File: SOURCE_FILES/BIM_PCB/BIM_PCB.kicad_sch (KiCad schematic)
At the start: 13 parts, among them J1 POWER INPUT, J6 Conn_01x04, Q1 SSM3J328R-HXY

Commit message: updates on schematic and complete layout
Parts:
- removed J6: Conn_01x04, Connector_Phoenix_MC:PhoenixContact_MC_1,5_4-G-3.5_1x04_P3.50mm_Horizontal, symbol Connector_Generic:Conn_01x04
- removed JP4, JP5: Jumper_3_Bridged12, Connector_PinHeader_2.54mm:PinHeader_1x03_P2.54mm_Vertical, symbol Jumper:Jumper_3_Bridged12
- added J6: Conn_02x02_Odd_Even, Connector_Molex:Molex_Mini-Fit_Jr_5569-04A2_2x02_P4.20mm_Horizontal, symbol Connector_Generic:Conn_02x02_Odd_Even
- gave numbers to parts that had none: 4
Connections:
- net +5V: now also J6.2 (Pin_2)
- net GND: now also J6.4 (Pin_4)
- net RS485_MAX485/A: now also J6.1 (Pin_1)
- net RS485_MAX485/B: now also J6.3 (Pin_3)
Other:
- sheet CAN_TRANSCEIVER_ATA6561 ports: added none; removed CANH, CANL
- sheet RS485_MAX485 ports: added RS485_DE, RS485_~{RE}; removed RS485_EN
- sheet SIM7000_GPRS_MODULE ports: added GPS_RXD, GPS_TXD; removed none
- sheet STM32FC8T6_MCU ports: added RS485_DE, RS485_~{RE}; removed RS485_EN

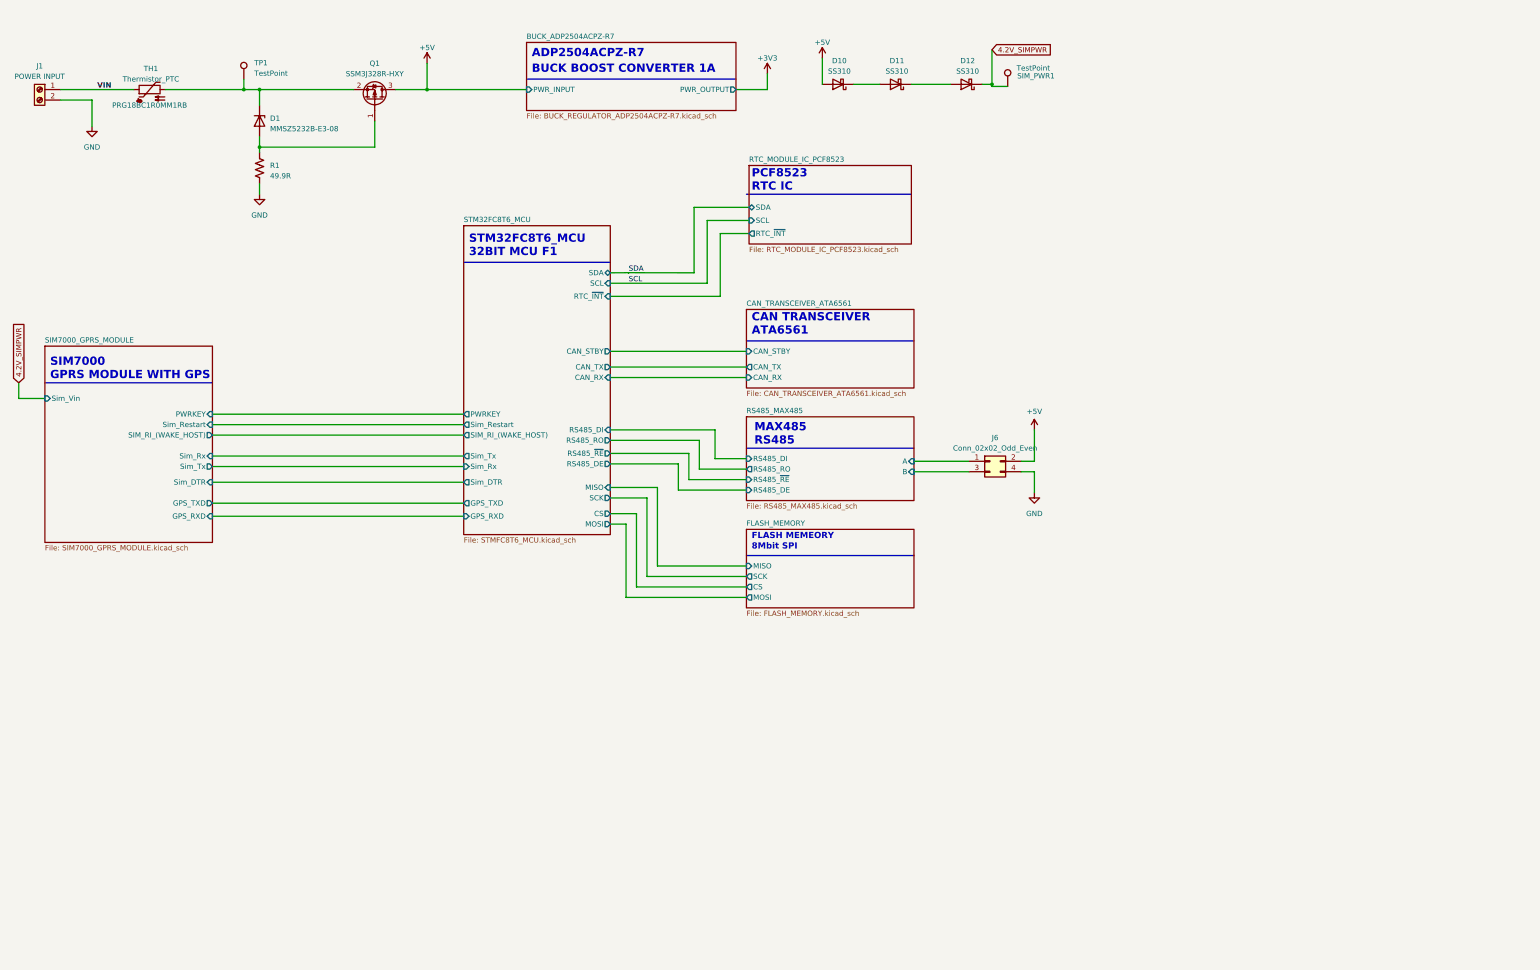
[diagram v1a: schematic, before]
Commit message: completed design PCN and Images
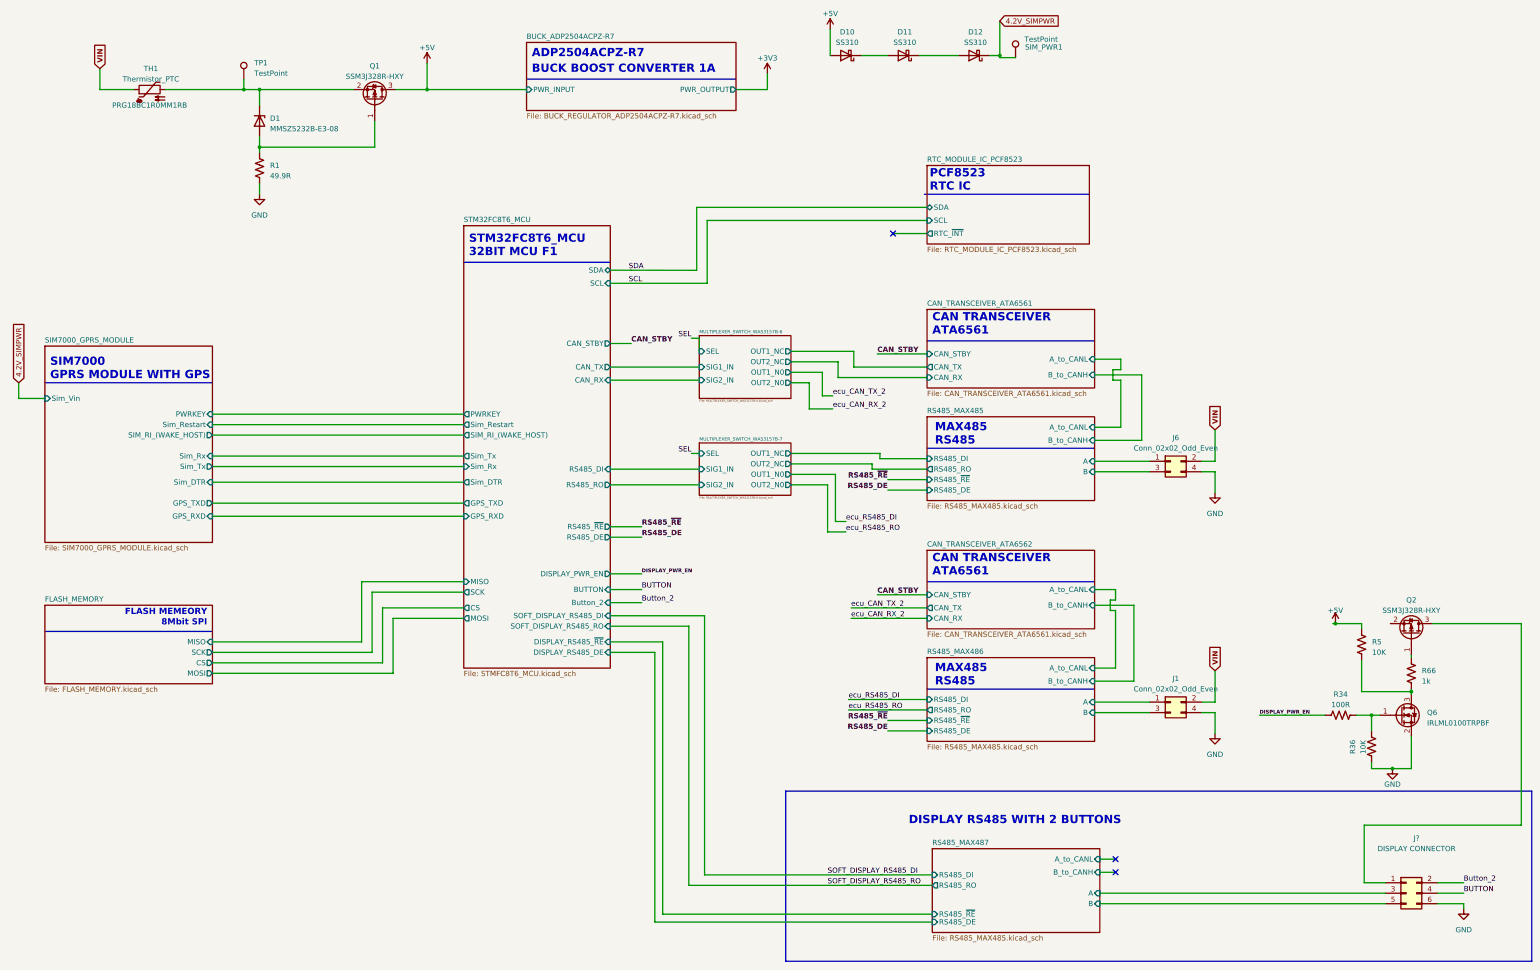
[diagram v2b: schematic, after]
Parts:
- removed J1: POWER INPUT, TerminalBlock_Phoenix:TerminalBlock_Phoenix_PT-1,5-2-3.5-H_1x02_P3.50mm_Horizontal, symbol Connector:Screw_Terminal_01x02
- added J1: Conn_02x02_Odd_Even, Connector_Molex:Molex_Nano-Fit_105314-xx04_2x02_P2.50mm_Horizontal, symbol Connector_Generic:Conn_02x02_Odd_Even
- added J?: DISPLAY CONNECTOR, Connector_Molex:Molex_Nano-Fit_105314-xx06_2x03_P2.50mm_Horizontal, symbol Connector_Generic:Conn_02x03_Odd_Even
- added Q2: SSM3J328R-HXY, Package_TO_SOT_SMD:SOT-23, symbol Device:Q_PMOS_GSD
- added Q6: IRLML0100TRPBF, Package_TO_SOT_SMD:SOT-23, symbol Device:Q_NMOS_GSD
- added R34: 100R, Resistor_SMD:R_0402_1005Metric, symbol Device:R_US
- added R36, R5: 10K, Resistor_SMD:R_0402_1005Metric, symbol Device:R_US
- added R66: 1k, Resistor_SMD:R_0402_1005Metric, symbol Device:R_US
- D1: footprint Diode_SMD:D_MiniMELF -> Diode_SMD:D_SOD-123
- J6: footprint Connector_Molex:Molex_Mini-Fit_Jr_5569-04A2_2x02_P4.20mm_Horizontal -> Connector_Molex:Molex_Nano-Fit_105314-xx04_2x02_P2.50mm_Horizontal
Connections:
- net +5V: now also R5.1; no longer J6.2 (Pin_2)
- net GND: now also J1.4 (Pin_4), J?.6 (Pin_6), Q6.2 (S), R36.2
- net VIN: now also J6.2 (Pin_2), J1.2 (Pin_2)
- new net: Q6.3 (D), R5.2, R66.1
- new net: Q6.1 (G), R34.1, R36.1
- new net: J?.1 (Pin_1), Q2.3 (D)
- new net: Q2.1 (G), R66.2
- new net BUTTON: J?.4 (Pin_4)
- new net Button_2: J?.2 (Pin_2)
- new net DISPLAY_PWR_EN: R34.2
- new net RS485_MAX486/A: J1.1 (Pin_1)
- new net RS485_MAX486/B: J1.3 (Pin_3)
- new net RS485_MAX487/A: J?.3 (Pin_3)
- new net RS485_MAX487/B: J?.5 (Pin_5)
- no-connect marks 0 -> 3
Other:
- added sheet CAN_TRANSCEIVER_ATA6562 (CAN_TRANSCEIVER_ATA6561.kicad_sch)
- added sheet MULTIPLEXER_SWITCH_WAS3157B-6 (MULTIPLEXER_SWITCH_WAS3157B-6.kicad_sch)
- added sheet MULTIPLEXER_SWITCH_WAS3157B-7 (MULTIPLEXER_SWITCH_WAS3157B-6.kicad_sch)
- added sheet RS485_MAX486 (RS485_MAX485.kicad_sch)
- added sheet RS485_MAX487 (RS485_MAX485.kicad_sch)
- sheet CAN_TRANSCEIVER_ATA6561 ports: added A_to_CANL, B_to_CANH; removed none
- sheet RS485_MAX485 ports: added A_to_CANL, B_to_CANH; removed none
- sheet STM32FC8T6_MCU ports: added BUTTON, Button_2, DISPLAY_PWR_EN, DISPLAY_RS485_DE, DISPLAY_RS485_~{RE}, SOFT_DISPLAY_RS485_DI, SOFT_DISPLAY_RS485_RO; removed RTC_~{INT}
- note added: "DISPLAY RS485 WITH 2 BUTTONS"
- moved on the sheet: D10, D11, D12, J6, SIM_PWR1

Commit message: complete BIM Board
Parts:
- added C45, C46: 100n, Capacitor_SMD:C_0603_1608Metric, symbol Device:C_Small
- added U14, U15: MC74HC4052A, Package_SO:SSOP-16_5.3x6.2mm_P0.65mm, symbol MCD_General:MC74HC4052A
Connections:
- net +3V3: now also C45.1, C46.1, U14.16 (VCC), U14.7 (VEE), U15.16 (VCC), U15.7 (VEE)
- net +5V: now also Q2.2 (S)
- net GND: now also C45.2, C46.2, U14.6 (ENABLE), U14.8 (GND), U15.6 (ENABLE), U15.8 (GND)
- net ecu_CAN_RX_2: now also U14.14 (X1)
- net ecu_CAN_TX_2: now also U14.5 (Y1)
- net ecu_RS485_DI: now also U15.5 (Y1)
- net ecu_RS485_RO: now also U15.14 (X1)
- new net CAN_RX_2: U14.12 (X0)
- new net CAN_TX_2: U14.1 (Y0)
- new net DISPLAY_RS485_DI: U15.2 (Y2)
- new net DISPLAY_RS485_RO: U15.15 (X2)
- new net MUX_SEL_A: U14.10 (A), U15.10 (A)
- new net MUX_SEL_B: U14.9 (B), U15.9 (B)
- new net RS485_D1: U15.1 (Y0)
- new net RS485_RO: U15.12 (X0)
- new net STM32FC8T6_MCU/CAN_RX: U14.13 (X)
- new net STM32FC8T6_MCU/CAN_TX: U14.3 (Y)
- new net STM32FC8T6_MCU/RS485_DI: U15.3 (Y)
- new net STM32FC8T6_MCU/RS485_RO: U15.13 (X)
- no-connect marks 3 -> 9
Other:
- removed sheet MULTIPLEXER_SWITCH_WAS3157B-6
- removed sheet MULTIPLEXER_SWITCH_WAS3157B-7
- sheet STM32FC8T6_MCU ports: added MUX_SEL_A, MUX_SEL_B, SEL; removed DISPLAY_RS485_DE, DISPLAY_RS485_~{RE}, SOFT_DISPLAY_RS485_DI, SOFT_DISPLAY_RS485_RO
- moved on the sheet: J1, J6, J?, Q2, Q6, R34, R36, R5, R66

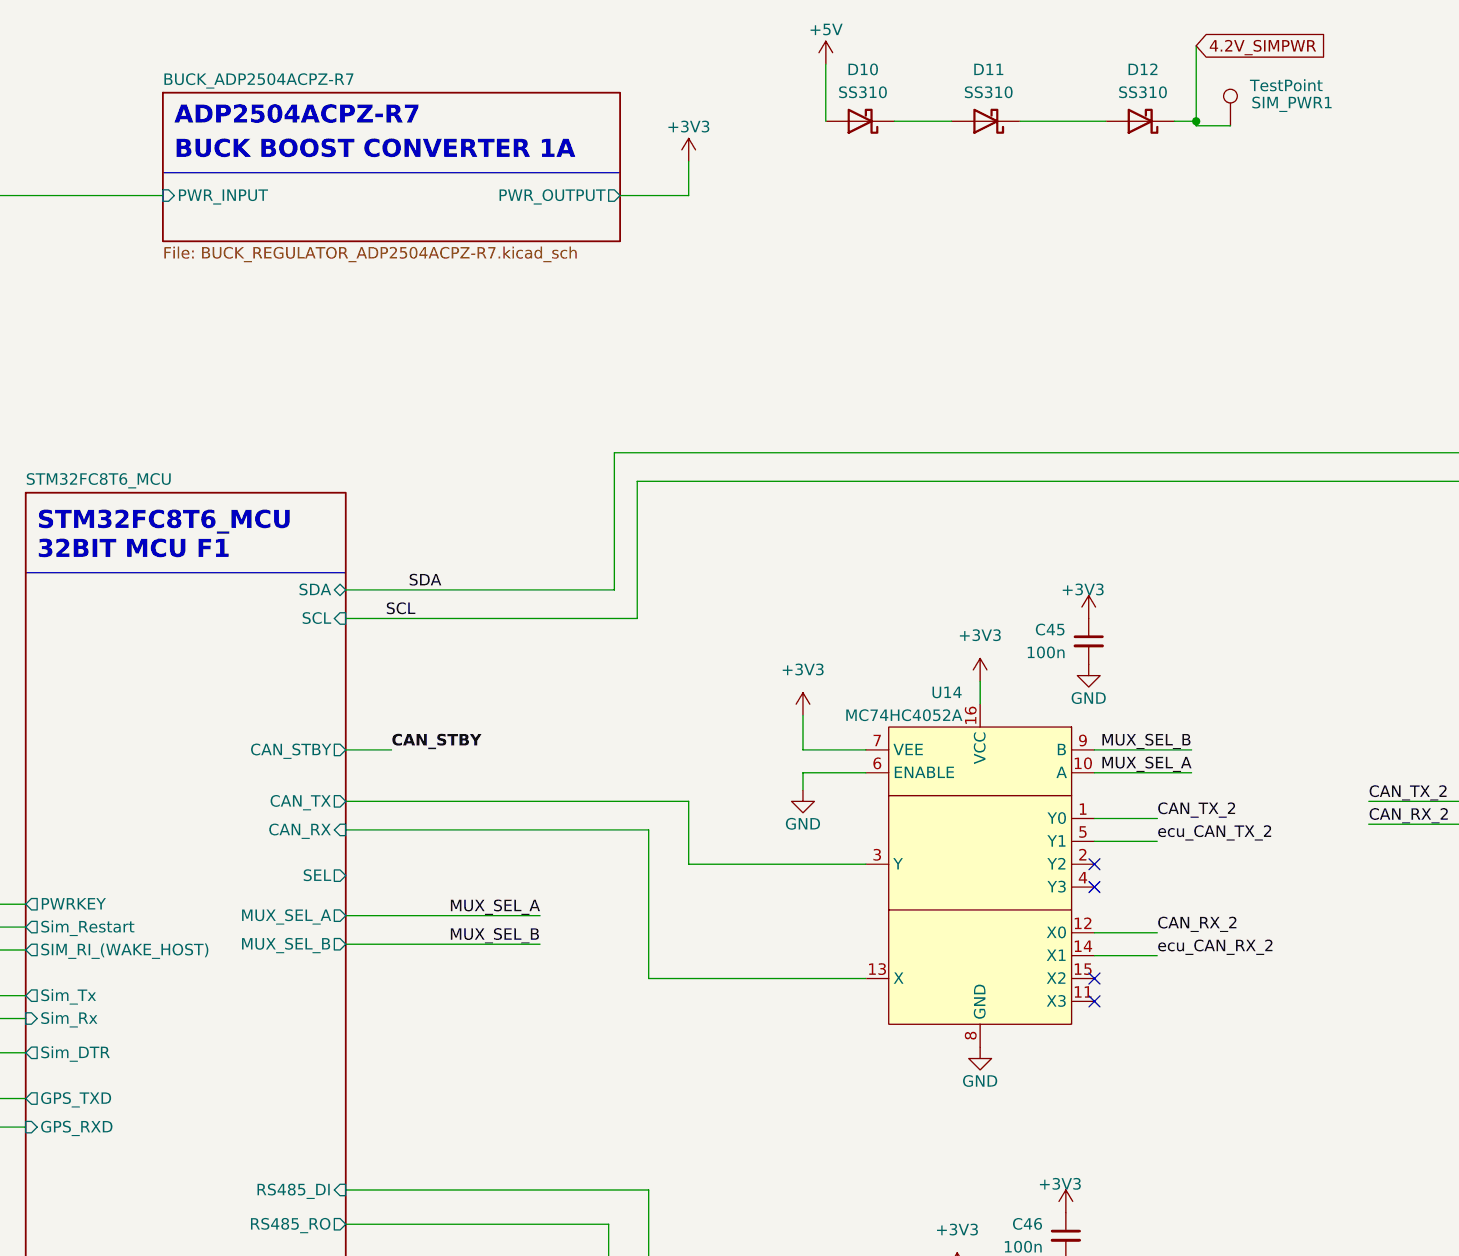
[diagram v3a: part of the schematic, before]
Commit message: updates on the buck 3v3 supply
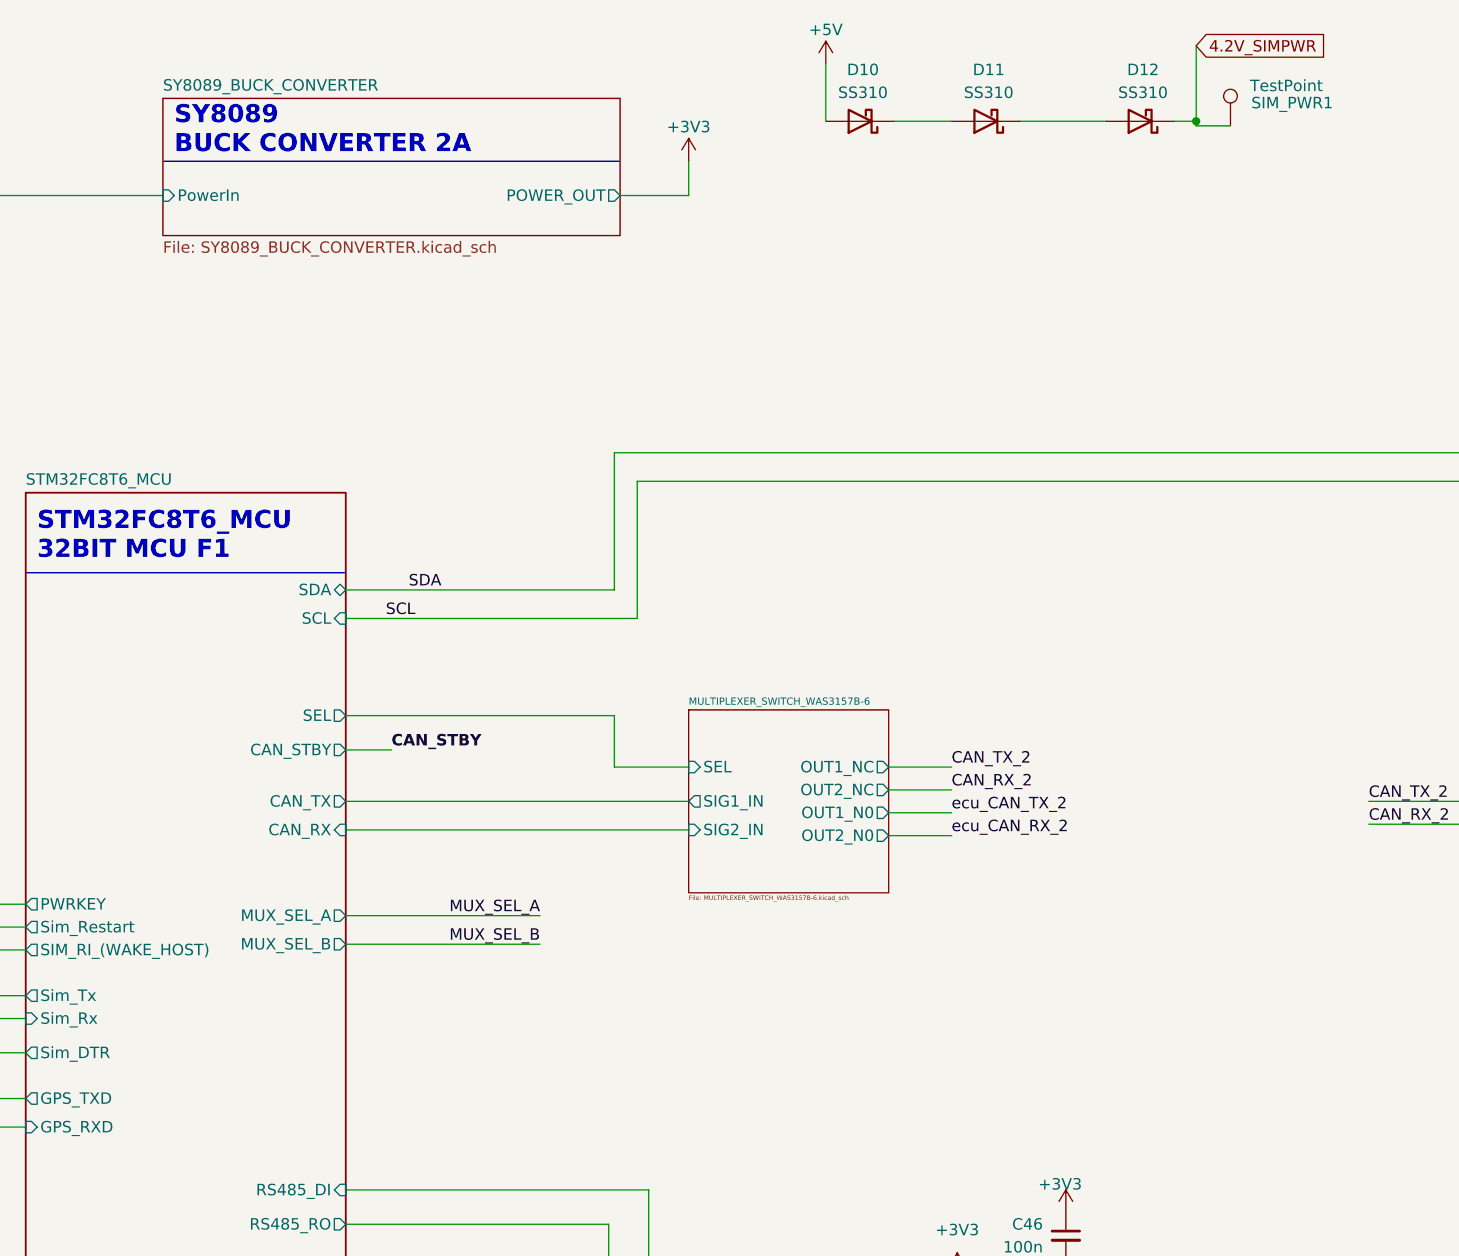
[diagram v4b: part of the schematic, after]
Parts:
- removed C45: 100n, Capacitor_SMD:C_0603_1608Metric, symbol Device:C_Small
- removed U14: MC74HC4052A, Package_SO:SSOP-16_5.3x6.2mm_P0.65mm, symbol MCD_General:MC74HC4052A
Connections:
- no-connect marks 9 -> 5
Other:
- removed sheet BUCK_ADP2504ACPZ-R7
- added sheet MULTIPLEXER_SWITCH_WAS3157B-6 (MULTIPLEXER_SWITCH_WAS3157B-6.kicad_sch)
- added sheet SY8089_BUCK_CONVERTER (SY8089_BUCK_CONVERTER.kicad_sch)
- note added: "SY8089 BUCK CONVERTER 2A"
- note removed: "ADP2504ACPZ-R7"
- note removed: "BUCK BOOST CONVERTER 1A"

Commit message: update to A9G and connector
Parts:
- removed J1, J6: Conn_02x02_Odd_Even, Connector_Molex:Molex_Nano-Fit_105314-xx04_2x02_P2.50mm_Horizontal, symbol Connector_Generic:Conn_02x02_Odd_Even
- removed J?: DISPLAY CONNECTOR, Connector_Molex:Molex_Nano-Fit_105314-xx06_2x03_P2.50mm_Horizontal, symbol Connector_Generic:Conn_02x03_Odd_Even
- added J1: Conn_02x09_Counter_Clockwise, Connector_Molex:Molex_Mini-Fit_Jr_5569-18A2_2x09_P4.20mm_Horizontal, symbol Connector_Generic:Conn_02x09_Counter_Clockwise
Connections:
- net BUTTON: now also J1.13 (Pin_13)
- net Button_2: now also J1.14 (Pin_14)
- net GND: now also J1.10 (Pin_10), J1.11 (Pin_11), J1.9 (Pin_9)
- net VIN: now also J1.1 (Pin_1), J1.18 (Pin_18)
- net at Q2.3 (D): now also J1.4 (Pin_4)
- new net DIS_A: J1.5 (Pin_5)
- new net DIS_B: J1.6 (Pin_6)
- new net ECU_A: J1.2 (Pin_2)
- new net ECU_B: J1.3 (Pin_3)
- new net RESET: J1.15 (Pin_15)
- new net RS485_A: J1.17 (Pin_17)
- new net RS485_B: J1.16 (Pin_16)
- new net SW0: J1.7 (Pin_7)
- new net swdclk: J1.12 (Pin_12)
- new net swdio: J1.8 (Pin_8)
- no-connect marks 5 -> 6
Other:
- removed sheet SIM7000_GPRS_MODULE
- added sheet A9G_GSM_GPRS_MODULE (A9G_GSM_GPRS_MODULE.kicad_sch)
- sheet STM32FC8T6_MCU ports: added RESET, SW0, swdclk, swdio; removed SIM_RI_(WAKE_HOST)
- note added: "A9G GPRS MODULE WITH GPS"
- note removed: "SIM7000 GPRS MODULE WITH GPS"
- moved on the sheet: C46, U15

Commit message: updated GENERAL
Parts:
- J1: MPN (none) -> 39301180
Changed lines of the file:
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@@
       (effects (font (size 1.27 1.27)) hide)
+    )
+    (property "MPN" "39301180" (at 391.16 216.535 0)
+      (effects (font (size 1.27 1.27)))
     )
     (pin "1")
@@
       (effects (font (size 1.27 1.27)) (justify right))
     )
-    (pin "GPS_TXD" output (at 66.04 111.125 0)
-      (effects (font (size 1.27 1.27)) (justify right))
-    )
-    (pin "GPS_RXD" input (at 66.04 114.3 0)
-      (effects (font (size 1.27 1.27)) (justify right))
-    )
-    (pin "Sim_Rx" input (at 66.04 101.6 0)
-      (effects (font (size 1.27 1.27)) (justify right))
-    )
-    (pin "Sim_Tx" output (at 66.04 99.06 0)
-      (effects (font (size 1.27 1.27)) (justify right))
-    )
+    (pin "GPS_TXD" output (at 66.04 114.3 0)
+      (effects (font (size 1.27 1.27)) (justify right))
+    )
+    (pin "GPS_RXD" input (at 66.04 111.125 0)
+      (effects (font (size 1.27 1.27)) (justify right))
+    )
+    (pin "Sim_Rx" input (at 66.04 99.06 0)
+      (effects (font (size 1.27 1.27)) (justify right))
+    )
+    (pin "Sim_Tx" output (at 66.04 101.6 0)
+      (effects (font (size 1.27 1.27)) (justify right))
+    )

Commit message: completed project
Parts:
- J1: footprint Connector_Molex:Molex_Mini-Fit_Jr_5569-18A2_2x09_P4.20mm_Horizontal -> MACHADA_footprints:conn_18pin_02x09_angled_MX23A18NF1; MPN 39301180 -> MX23A18NF1
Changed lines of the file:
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@@
       (effects (font (size 1.27 1.27)))
     )
-    (property "Footprint" "Connector_Molex:Molex_Mini-Fit_Jr_5569-18A2_2x09_P4.20mm_Horizontal" (at 375.92 229.87 0)
+    (property "Footprint" "MACHADA_footprints:conn_18pin_02x09_angled_MX23A18NF1" (at 375.92 229.87 0)
       (effects (font (size 1.27 1.27)) hide)
     )
@@
       (effects (font (size 1.27 1.27)) hide)
     )
-    (property "MPN" "39301180" (at 391.16 216.535 0)
+    (property "MPN" "MX23A18NF1" (at 391.16 216.535 0)
       (effects (font (size 1.27 1.27)))
     )
